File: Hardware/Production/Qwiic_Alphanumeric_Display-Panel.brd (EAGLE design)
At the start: 240.5 x 155.4 mm, 1078 parts, among them J11 Vertical Qwiic Connector, J12 Vertical Qwiic Connector, J14 Vertical Qwiic Connector, J15 Vertical Qwiic Connector, J17 Vertical Qwiic Connector, J18 Vertical Qwiic Connector, J2 Vertical Qwiic Connector, J20 Vertical Qwiic Connector, J21 Vertical Qwiic Connector, J23 Vertical Qwiic Connector, J24 Vertical Qwiic Connector, J26 Vertical Qwiic Connector, J27 Vertical Qwiic Connector, J29 Vertical Qwiic Connector, J30 Vertical Qwiic Connector, J32 Vertical Qwiic Connector, J33 Vertical Qwiic Connector, J35 Vertical Qwiic Connector, J36 Vertical Qwiic Connector, J38 Vertical Qwiic Connector, J39 Vertical Qwiic Connector, J4 Vertical Qwiic Connector, J41 Vertical Qwiic Connector, J42 Vertical Qwiic Connector, J44 Vertical Qwiic Connector, J45 Vertical Qwiic Connector, J47 Vertical Qwiic Connector, J48 Vertical Qwiic Connector, J5 Vertical Qwiic Connector, J50 Vertical Qwiic Connector, J51 Vertical Qwiic Connector, J53 Vertical Qwiic Connector, J54 Vertical Qwiic Connector, J56 Vertical Qwiic Connector, J57 Vertical Qwiic Connector, J59 Vertical Qwiic Connector, J6 Vertical Qwiic Connector, J60 Vertical Qwiic Connector, J62 Vertical Qwiic Connector, J63 Vertical Qwiic Connector, J65 Vertical Qwiic Connector, J66 Vertical Qwiic Connector, J68 Vertical Qwiic Connector, J69 Vertical Qwiic Connector, J71 Vertical Qwiic Connector, J72 Vertical Qwiic Connector, J74 Vertical Qwiic Connector, J75 Vertical Qwiic Connector, J8 Vertical Qwiic Connector, J9 Vertical Qwiic Connector

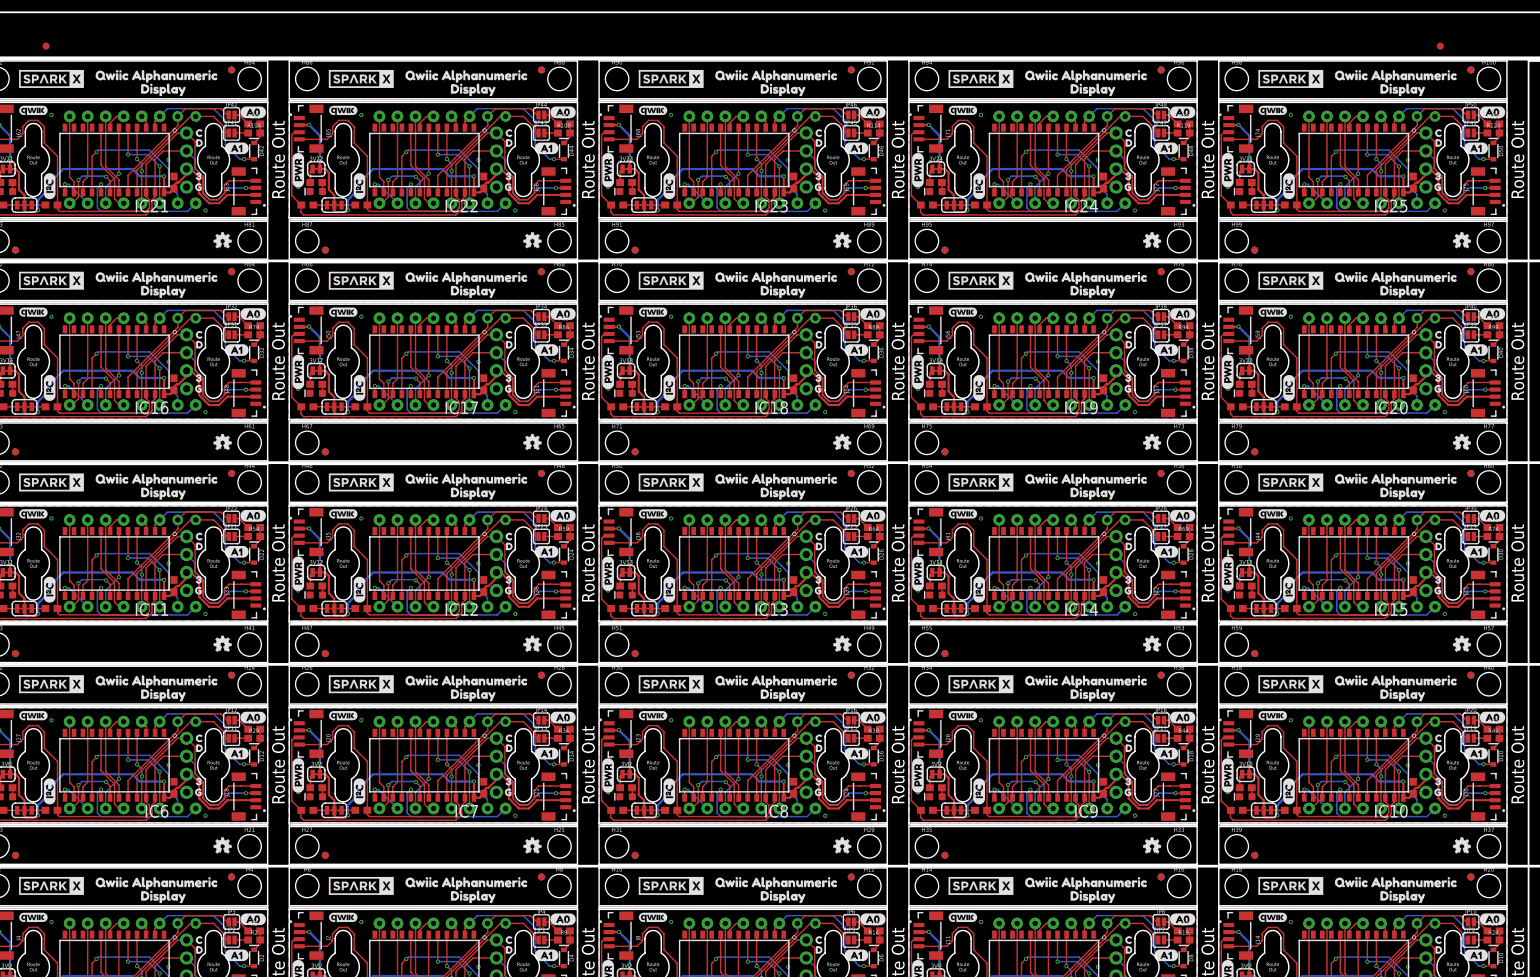
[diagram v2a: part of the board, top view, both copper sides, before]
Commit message: New decoupling cap
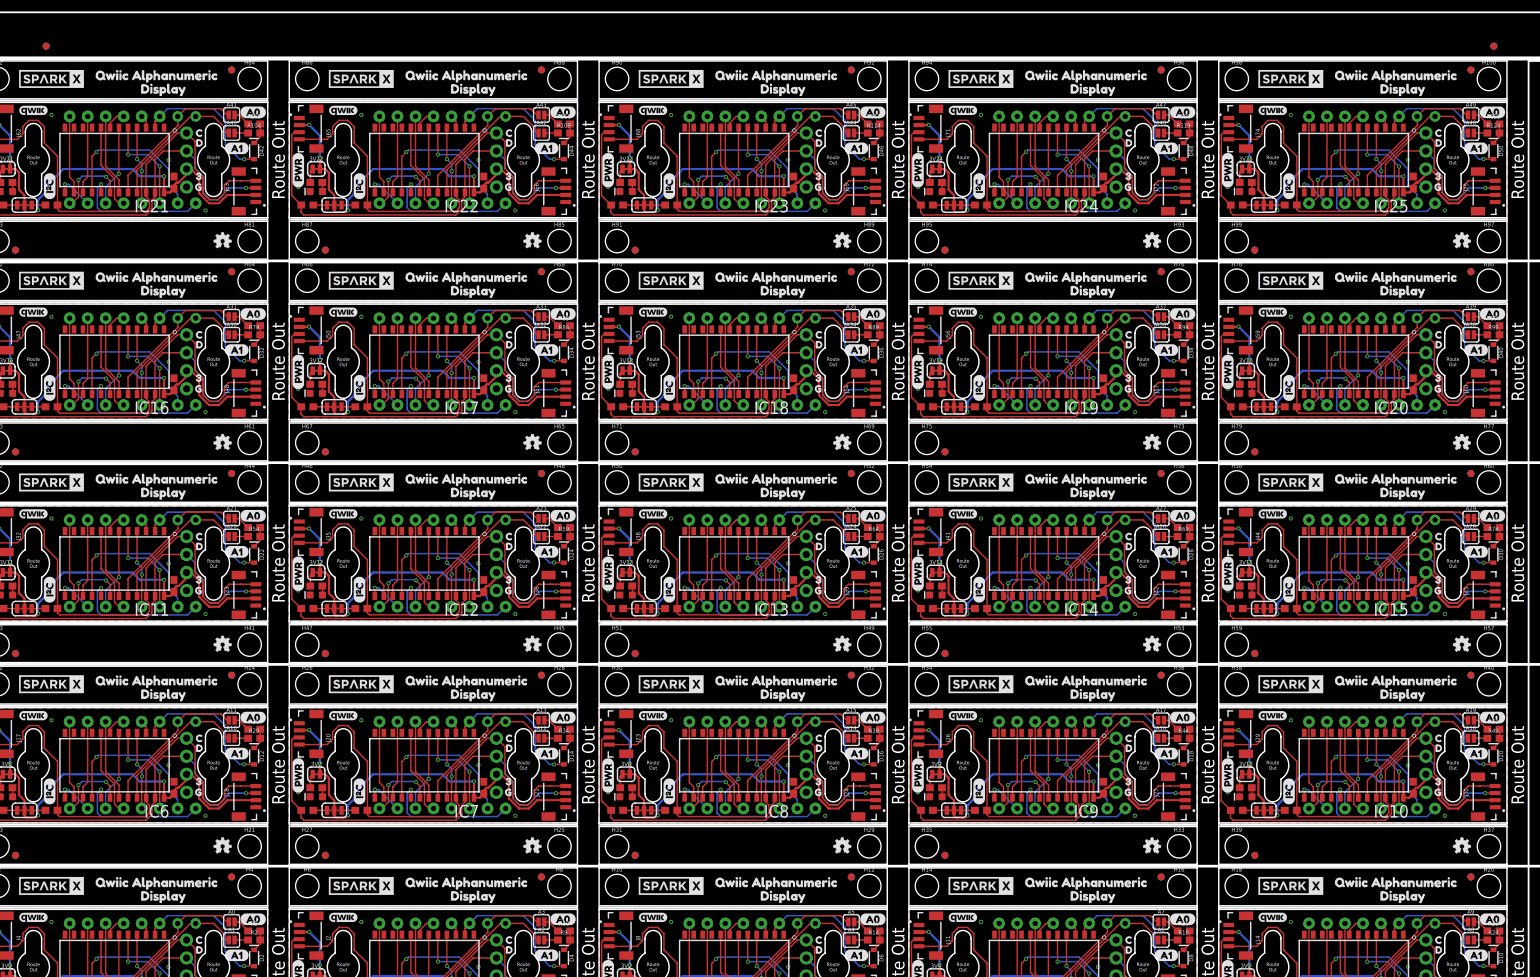
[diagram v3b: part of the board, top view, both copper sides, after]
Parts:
- added E$4: (no value), SparkFun-Aesthetics:FIDUCIAL-1X2
- added E$5: (no value), SparkFun-Retired:FIDUCIAL-1.5X3
- C1, C10, C11, C12, C13, C14, C15, C16, C17, C18, C19, C2, C20, C21, C22, C23, C24, C25, C3, C4, C5, C6, C7, C8, C9: value 0.1uF -> 1.0uF
- E$3: device SparkFun-Retired:FIDUCIAL-1.5X3 -> SparkFun-Aesthetics:FIDUCIAL-1X2
- moved E$3 250.9 mm to (213.6, 143.8)
- moved E$2 196.6 mm to (9.40, 143.8), flipped to the bottom
- renumbered JP1 to A2, JP10 to A9, JP11 to A10, JP12 to A11, JP13 to A12, JP14 to A13, JP15 to A14, JP16 to A15, JP17 to A16, JP18 to A17, JP19 to A18, JP2 to A1, JP20 to A19, JP21 to A20, JP22 to A21, JP23 to A22, JP24 to A23, JP25 to A24, JP26 to A25, JP27 to A26, JP28 to A27, JP29 to A28, JP3 to A0, JP30 to A29, JP31 to A30, JP32 to A31, JP33 to A32, JP34 to A33, JP35 to A34, JP36 to A35, JP37 to A36, JP38 to A37, JP39 to A38, JP4 to A3, JP40 to A39, JP41 to A40, JP42 to A41, JP43 to A42, JP44 to A43, JP45 to A44, JP46 to A45, JP47 to A46, JP48 to A47, JP49 to A48, JP5 to A4, JP50 to A49, JP6 to A5, JP7 to A6, JP8 to A7, JP9 to A8

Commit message: Added extra decoupling cap
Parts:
- added C26, C28, C30, C32, C34, C36, C38, C40, C42, C44, C46, C48, C50: 10uF, SparkFun-Capacitors:0603
- added C27, C29, C31, C33, C35, C37, C39, C41, C43, C45, C47, C49: 0.1uF, SparkFun-Capacitors:0603
- C1, C11, C13, C15, C17, C19, C21, C23, C25, C3, C5, C7, C9: value 1.0uF -> 0.1uF
- C10, C12, C14, C16, C18, C2, C20, C22, C24, C4, C6, C8: value 1.0uF -> 10uF
- moved C17 104.3 mm to (158.5, 39.2)
- moved C25 104.3 mm to (114.8, 67.7)
- moved C16 101.0 mm to (114.8, 45.5)
- moved C24 101.0 mm to (71.1, 73.9)
- moved C7 91.9 mm to (158.5, 10.8)
- moved C15 91.9 mm to (114.8, 39.2)
- moved C14 90.2 mm to (71.1, 45.5)
- moved C6 90.2 mm to (114.8, 17.0)
- moved C4 87.6 mm to (71.1, 17.0)
- moved C5 87.4 mm to (114.8, 10.8)
- moved C23 71.7 mm to (71.1, 67.7)
- moved C19 71.7 mm to (202.2, 39.2)
- moved C18 66.9 mm to (158.5, 45.5)
- moved C22 66.9 mm to (27.4, 73.9)
- moved C21 56.9 mm to (27.4, 67.7)
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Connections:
- net 3.3V: now also C2.1
- net 3.3V1: now also C3.1, C4.1; no longer C2.1
- net 3.3V10: now also C21.1, C22.1; no longer C11.1
- net 3.3V11: now also C23.1, C24.1; no longer C12.1
- net 3.3V12: now also C25.1, C26.1; no longer C13.1
- net 3.3V13: now also C27.1, C28.1; no longer C14.1
- net 3.3V14: now also C29.1, C30.1; no longer C15.1
- net 3.3V15: now also C31.1, C32.1; no longer C16.1
- net 3.3V16: now also C33.1, C34.1; no longer C17.1
- net 3.3V17: now also C35.1, C36.1; no longer C18.1
- net 3.3V18: now also C37.1, C38.1; no longer C19.1
- net 3.3V19: now also C39.1, C40.1; no longer C20.1
- net 3.3V2: now also C5.1, C6.1; no longer C3.1
- net 3.3V20: now also C41.1, C42.1; no longer C21.1
- net 3.3V21: now also C43.1, C44.1; no longer C22.1
- net 3.3V22: now also C45.1, C46.1; no longer C23.1
- net 3.3V23: now also C47.1, C48.1; no longer C24.1
- net 3.3V24: now also C49.1, C50.1; no longer C25.1
- net 3.3V3: now also C7.1, C8.1; no longer C4.1
- net 3.3V4: now also C10.1, C9.1; no longer C5.1
- net 3.3V5: now also C11.1, C12.1; no longer C6.1
- net 3.3V6: now also C13.1, C14.1; no longer C7.1
- net 3.3V7: now also C15.1, C16.1; no longer C8.1
- net 3.3V8: now also C17.1, C18.1; no longer C9.1
- net 3.3V9: now also C19.1, C20.1; no longer C10.1
- net GND: now also C2.2
- net GND1: now also C3.2, C4.2; no longer C2.2
- net GND10: now also C21.2, C22.2; no longer C11.2
- net GND11: now also C23.2, C24.2; no longer C12.2
- net GND12: now also C25.2, C26.2; no longer C13.2
- net GND13: now also C27.2, C28.2; no longer C14.2
- net GND14: now also C29.2, C30.2; no longer C15.2
- net GND15: now also C31.2, C32.2; no longer C16.2
- net GND16: now also C33.2, C34.2; no longer C17.2
- net GND17: now also C35.2, C36.2; no longer C18.2
- net GND18: now also C37.2, C38.2; no longer C19.2
- net GND19: now also C39.2, C40.2; no longer C20.2
- net GND2: now also C5.2, C6.2; no longer C3.2
- net GND20: now also C41.2, C42.2; no longer C21.2
- net GND21: now also C43.2, C44.2; no longer C22.2
- net GND22: now also C45.2, C46.2; no longer C23.2
- net GND23: now also C47.2, C48.2; no longer C24.2
- net GND24: now also C49.2, C50.2; no longer C25.2
- net GND3: now also C7.2, C8.2; no longer C4.2
- net GND4: now also C10.2, C9.2; no longer C5.2
- net GND5: now also C11.2, C12.2; no longer C6.2
- net GND6: now also C13.2, C14.2; no longer C7.2
- net GND7: now also C15.2, C16.2; no longer C8.2
- net GND8: now also C17.2, C18.2; no longer C9.2
- net GND9: now also C19.2, C20.2; no longer C10.2
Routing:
- net 3.3V19: track 60.6 -> 64.8 mm
- net 3.3V17: track 60.6 -> 64.8 mm
- net 3.3V15: track 60.6 -> 64.8 mm
- net 3.3V: track 60.6 -> 64.8 mm
- net 3.3V8: track 60.6 -> 64.8 mm
- net 3.3V7: track 60.6 -> 64.8 mm
- net 3.3V6: track 60.6 -> 64.8 mm
- net 3.3V5: track 60.6 -> 64.8 mm
- net 3.3V3: track 60.6 -> 64.8 mm
- net 3.3V23: track 60.6 -> 64.8 mm
- net 3.3V22: track 60.6 -> 64.8 mm
- net 3.3V21: track 60.6 -> 64.8 mm
- net 3.3V20: track 60.6 -> 64.8 mm
- net 3.3V2: track 60.6 -> 64.8 mm
- net 3.3V16: track 60.6 -> 64.8 mm
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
